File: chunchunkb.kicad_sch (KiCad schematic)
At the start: 116 parts, among them J1 Conn_01x02, SW1 SW_Push, SW10 SW_Push, SW11 SW_Push, SW12 SW_Push, SW13 SW_Push, SW14 SW_Push, SW15 SW_Push, SW16 SW_Push, SW17 SW_Push, SW18 SW_Push, SW19 SW_Push, SW2 SW_Push, SW20 SW_Push, SW21 SW_Push, SW22 SW_Push, SW23 SW_Push, SW24 SW_Push, SW25 SW_Push, SW26 SW_Push, SW27 SW_Push, SW28 SW_Push, SW29 SW_Push, SW3 SW_Push, SW30 SW_Push, SW31 EC11, SW32 SW_Push, SW33 SW_Push, SW34 SW_Push, SW35 SW_Push, SW36 SW_Push, SW4 SW_Push, SW5 SW_Push, SW6 SW_Push, SW7 SW_Push, SW8 SW_Push, SW9 SW_Push

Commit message: chore: reroute
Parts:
- LED1, LED10, LED11, LED12, LED13, LED14, LED15, LED16, LED17, LED18, LED19, LED2, LED20, LED21, LED22, LED23, LED24, LED25, LED26, LED27, LED28, LED29, LED3, LED30, LED31, LED32, LED33, LED34, LED35, LED4, LED5, LED6, LED7, LED8, LED9: value SK6812MINI-E -> YS-SK6812MINI-E
- SW31: footprint Rotary_Encoder:RotaryEncoder_Alps_EC11E-Switch_Vertical_H20mm -> kbd:keyswitch_cherrymx_hotswap_1u_rotary_encoder_ec12
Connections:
- net at LED13.2 (DOUT): now also LED14.4 (DIN); no longer LED12.2 (DOUT)
- net at LED31.4 (DIN): now also LED30.2 (DOUT); no longer LED30.4 (DIN)
- net at LED26.2 (DOUT): now also LED27.4 (DIN); no longer LED25.4 (DIN)
- net at LED27.2 (DOUT): now also LED28.4 (DIN); no longer LED26.4 (DIN)
- net at LED19.4 (DIN): now also LED18.2 (DOUT); no longer LED18.4 (DIN)
- net at LED25.2 (DOUT): now also LED26.4 (DIN); no longer LED24.2 (DOUT)
- net at LED15.2 (DOUT): now also LED16.4 (DIN); no longer LED14.4 (DIN)
- net at LED15.4 (DIN): now also LED14.2 (DOUT); no longer LED16.2 (DOUT)
- net at LED29.4 (DIN): now also LED28.2 (DOUT); no longer LED30.2 (DOUT)
- net at LED29.2 (DOUT): now also LED30.4 (DIN); no longer LED28.4 (DIN)
- net at LED13.4 (DIN): now also LED12.2 (DOUT); no longer LED14.2 (DOUT)
- net at LED17.4 (DIN): now also LED16.2 (DOUT); no longer LED18.2 (DOUT)
- net at LED17.2 (DOUT): now also LED18.4 (DIN); no longer LED16.4 (DIN)
- new net: LED24.2 (DOUT), LED25.4 (DIN)

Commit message: dual pcb
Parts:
- added D37, D38, D39, D40, D41, D42, D43, D44, D45, D46, D47, D48, D49, D50, D51, D52, D53, D54, D55, D56, D57, D58, D59, D60, D61, D62, D63, D64, D65, D66, D67, D68, D69, D70, D71, D72: 1N4148W, Diode_SMD:D_SOD-123, symbol Diode:1N4148W
- added Display2: nice!view, chunchunkb:nice_view, symbol nice_view:nice!view
- added H5, H6, H7, H8: MountingHole, MountingHole:MountingHole_2.2mm_M2_Pad, symbol Mechanical:MountingHole
- added J2: Conn_01x02, Connector_Molex:Molex_CLIK-Mate_502382-0270_1x02-1MP_P1.25mm_Vertical, symbol Connector_Generic:Conn_01x02
- added LED36, LED37, LED38, LED39, LED40, LED41, LED42, LED43, LED44, LED45, LED46, LED47, LED48, LED49, LED50, LED51, LED52, LED53, LED54, LED55, LED56, LED57, LED58, LED59, LED60, LED61, LED62, LED63, LED64, LED65, LED66, LED67, LED68, LED69, LED70: YS-SK6812MINI-E, chunchunkb:kbd.YS-SK6812MINI-E, symbol kbd:YS-SK6812MINI-E
- added MCU2: nice_nano, chunchunkb:kbd.ProMicro, symbol nice_nano:nice_nano
- added SW37, SW38, SW39, SW40, SW41, SW42, SW43, SW44, SW45, SW46, SW47, SW48, SW49, SW50, SW51, SW52, SW53, SW54, SW55, SW56, SW57, SW58, SW59, SW60, SW61, SW62, SW63, SW64, SW65, SW66, SW68, SW69, SW70, SW71, SW72: SW_Push, chunchunkb:kbd.keyswitch_cherrymx_hotswap_1u, symbol Switch:SW_Push
- added SW67: EC11, chunchunkb:RotaryEncoder_Alps_EC11E-Switch_Vertical_H20mm, symbol Device:RotaryEncoder_Switch
- added SW_POWER2: SW_SPDT, Button_Switch_SMD:SW_SPDT_PCM12, symbol Switch:SW_SPDT
- added SW_RST2: SW_Push, Button_Switch_SMD:SW_Tactile_SPST_NO_Straight_CK_PTS636Sx25SMTRLFS, symbol Switch:SW_Push
- Display1: footprint nice_view:nice_view -> chunchunkb:nice_view
- LED1, LED10, LED11, LED12, LED13, LED14, LED15, LED16, LED17, LED18, LED19, LED2, LED20, LED21, LED22, LED23, LED24, LED25, LED26, LED27, LED28, LED29, LED3, LED30, LED31, LED32, LED33, LED34, LED35, LED4, LED5, LED6, LED7, LED8, LED9: footprint kbd:YS-SK6812MINI-E -> chunchunkb:kbd.YS-SK6812MINI-E
- MCU1: footprint kbd:ProMicro -> chunchunkb:kbd.ProMicro
- SW1, SW10, SW11, SW12, SW13, SW14, SW15, SW16, SW17, SW18, SW19, SW2, SW20, SW21, SW22, SW23, SW24, SW25, SW26, SW27, SW28, SW29, SW3, SW30, SW32, SW33, SW34, SW35, SW36, SW4, SW5, SW6, SW7, SW8, SW9: footprint kbd:keyswitch_cherrymx_hotswap_1u -> chunchunkb:kbd.keyswitch_cherrymx_hotswap_1u
- SW31: footprint kbd:keyswitch_cherrymx_hotswap_1u_rotary_encoder_ec12 -> chunchunkb:RotaryEncoder_Alps_EC11E-Switch_Vertical_H20mm
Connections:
- net +BATT renamed +BATT L
- net COL 0 renamed COL 0 L
- net COL 1 renamed COL 1 L
- net COL 2 renamed COL 2 L
- net COL 3 renamed COL 3 L
- net COL 4 renamed COL 4 L
- net COL 5 renamed COL 5 L
- net CS renamed CS L
- net ENC A renamed ENC A L
- net ENC B renamed ENC B L
- net LED renamed LED L
- net MOSI renamed MOSI L
- net ROW 0 renamed ROW 0 L
- net ROW 1 renamed ROW 1 L
- net ROW 2 renamed ROW 2 L
- net ROW 3 renamed ROW 3 L
- net ROW 4 renamed ROW 4 L
- net ROW 5 renamed ROW 5 L
- net SCK renamed SCK L
- net VCC renamed VCC L
- new net: D58.2 (A), SW58.2
- new net: LED68.2 (DOUT), LED69.4 (DIN)
- new net: LED67.2 (DOUT), LED68.4 (DIN)
- new net: LED51.2 (DOUT), LED52.4 (DIN)
- new net: LED50.2 (DOUT), LED51.4 (DIN)
- new net: D70.2 (A), SW70.2
- new net: D38.2 (A), SW38.2
- new net: D55.2 (A), SW55.2
- new net: D59.2 (A), SW59.2
- new net: D62.2 (A), SW62.2
- new net: LED36.2 (DOUT), LED37.4 (DIN)
- new net: D37.2 (A), SW37.2
- new net: D42.2 (A), SW42.2
- new net: LED54.2 (DOUT), LED55.4 (DIN)
- new net: LED53.2 (DOUT), LED54.4 (DIN)
- new net: LED55.2 (DOUT), LED56.4 (DIN)
- new net: LED45.2 (DOUT), LED46.4 (DIN)
- new net: LED44.2 (DOUT), LED45.4 (DIN)
- new net: MCU2.22 (RST), SW_RST2.1
- new net: D60.2 (A), SW60.2
- new net: LED59.2 (DOUT), LED60.4 (DIN)
- new net: LED58.2 (DOUT), LED59.4 (DIN)
- new net: D44.2 (A), SW44.2
- new net: D46.2 (A), SW46.2
- new net: D72.2 (A), SW72.2
- new net: LED49.2 (DOUT), LED50.4 (DIN)
- new net: LED48.2 (DOUT), LED49.4 (DIN)
- new net: LED69.2 (DOUT), LED70.4 (DIN)
- new net: LED63.2 (DOUT), LED64.4 (DIN)
- new net: LED62.2 (DOUT), LED63.4 (DIN)
- new net: D43.2 (A), SW43.2
- new net: D56.2 (A), SW56.2
- new net: D52.2 (A), SW52.2
- new net: LED47.2 (DOUT), LED48.4 (DIN)
- new net: LED46.2 (DOUT), LED47.4 (DIN)
- new net: LED65.2 (DOUT), LED66.4 (DIN)
- new net: LED64.2 (DOUT), LED65.4 (DIN)
- new net: LED39.2 (DOUT), LED40.4 (DIN)
- new net: LED38.2 (DOUT), LED39.4 (DIN)
- new net: LED37.2 (DOUT), LED38.4 (DIN)
- new net: LED57.2 (DOUT), LED58.4 (DIN)
- new net: LED56.2 (DOUT), LED57.4 (DIN)
- new net: LED41.2 (DOUT), LED42.4 (DIN)
- new net: LED40.2 (DOUT), LED41.4 (DIN)
- new net: D68.2 (A), SW68.2
- new net: D48.2 (A), SW48.2
- new net: D63.2 (A), SW63.2
- new net: LED66.2 (DOUT), LED67.4 (DIN)
- new net: MCU2.24 (BATIN/P0.04), SW_POWER2.2 (B)
- new net: D66.2 (A), SW66.2
- new net: D69.2 (A), SW69.2
- new net: D54.2 (A), SW54.2
- new net: D40.2 (A), SW40.2
- new net: LED43.2 (DOUT), LED44.4 (DIN)
- new net: D39.2 (A), SW39.2
- new net: LED52.2 (DOUT), LED53.4 (DIN)
- new net: D50.2 (A), SW50.2
- new net: D49.2 (A), SW49.2
- new net: D61.2 (A), SW61.2
- new net: D41.2 (A), SW41.2
- new net: D65.2 (A), SW65.2
- new net: LED42.2 (DOUT), LED43.4 (DIN)
- new net: D53.2 (A), SW53.2
- new net: D71.2 (A), SW71.2
- new net: D64.2 (A), SW64.2
- new net: D47.2 (A), SW47.2
- new net: LED61.2 (DOUT), LED62.4 (DIN)
- new net: LED60.2 (DOUT), LED61.4 (DIN)
- new net: D45.2 (A), SW45.2
- new net: D51.2 (A), SW51.2
- new net: D57.2 (A), SW57.2
- new net +BATT R: J2.1 (Pin_1), SW_POWER2.1 (A)
- new net COL 0 R: MCU2.18 (AIN0/P0.02), SW37.1, SW43.1, SW49.1, SW55.1, SW61.1, SW67.S1
- new net COL 1 R: MCU2.17 (P1.15), SW38.1, SW44.1, SW50.1, SW56.1, SW62.1, SW68.1
- new net COL 2 R: MCU2.16 (P1.13), SW39.1, SW45.1, SW51.1, SW57.1, SW63.1, SW69.1
- new net COL 3 R: MCU2.15 (P1.11), SW40.1, SW46.1, SW52.1, SW58.1, SW64.1, SW70.1
- new net COL 4 R: MCU2.14 (NFC2/P0.10), SW41.1, SW47.1, SW53.1, SW59.1, SW65.1, SW71.1
- new net COL 5 R: MCU2.13 (NFC1/P0.09), SW42.1, SW48.1, SW54.1, SW60.1, SW66.1, SW72.1
- new net CS R: Display2.5 (CS), MCU2.5 (P0.17)
- new net ENC A R: MCU2.20 (AIN7/P0.31), SW67.A
- new net ENC B R: MCU2.19 (AIN5/P0.29), SW67.B
- new net GND R: Display2.4 (GND), J2.2 (Pin_2), LED36.3 (GND_R), LED37.3 (GND_R), LED38.3 (GND_R), LED39.3 (GND_R), LED40.3 (GND_R), LED41.3 (GND_R), LED42.3 (GND_R), LED43.3 (GND_R), LED44.3 (GND_R), LED45.3 (GND_R), LED46.3 (GND_R), LED47.3 (GND_R), LED48.3 (GND_R), LED49.3 (GND_R), LED50.3 (GND_R), LED51.3 (GND_R), LED52.3 (GND_R), LED53.3 (GND_R), LED54.3 (GND_R), LED55.3 (GND_R), LED56.3 (GND_R), LED57.3 (GND_R), LED58.3 (GND_R), LED59.3 (GND_R), LED60.3 (GND_R), LED61.3 (GND_R), LED62.3 (GND_R), LED63.3 (GND_R), LED64.3 (GND_R), LED65.3 (GND_R), LED66.3 (GND_R), LED67.3 (GND_R), LED68.3 (GND_R), LED69.3 (GND_R), LED70.3 (GND_R), MCU2.23 (GND), MCU2.3 (GND), MCU2.4 (GND), SW67.C, SW_RST2.2
- new net LED R: LED36.4 (DIN), MCU2.2 (RX1/P0.08)
- new net MOSI R: Display2.1 (MOSI), MCU2.1 (TX0/P0.06)
- new net ROW 0 R: D37.1 (K), D38.1 (K), D39.1 (K), D40.1 (K), D41.1 (K), D42.1 (K), MCU2.7 (P0.22)
- new net ROW 1 R: D43.1 (K), D44.1 (K), D45.1 (K), D46.1 (K), D47.1 (K), D48.1 (K), MCU2.8 (P0.24)
- new net ROW 2 R: D49.1 (K), D50.1 (K), D51.1 (K), D52.1 (K), D53.1 (K), D54.1 (K), MCU2.9 (P1.00)
- new net ROW 3 R: D55.1 (K), D56.1 (K), D57.1 (K), D58.1 (K), D59.1 (K), D60.1 (K), MCU2.10 (P0.11)
- new net ROW 4 R: D61.1 (K), D62.1 (K), D63.1 (K), D64.1 (K), D65.1 (K), D66.1 (K), MCU2.11 (P1.04)
- new net ROW 5 R: D67.1 (K), D68.1 (K), D69.1 (K), D70.1 (K), D71.1 (K), D72.1 (K), MCU2.12 (P1.06)
- new net SCK R: Display2.2 (SCK), MCU2.6 (P0.20)
- new net SW67B: D67.2 (A), SW67.S2
- new net VCC R: Display2.3 (VCC), LED36.1 (VDD_R), LED37.1 (VDD_R), LED38.1 (VDD_R), LED39.1 (VDD_R), LED40.1 (VDD_R), LED41.1 (VDD_R), LED42.1 (VDD_R), LED43.1 (VDD_R), LED44.1 (VDD_R), LED45.1 (VDD_R), LED46.1 (VDD_R), LED47.1 (VDD_R), LED48.1 (VDD_R), LED49.1 (VDD_R), LED50.1 (VDD_R), LED51.1 (VDD_R), LED52.1 (VDD_R), LED53.1 (VDD_R), LED54.1 (VDD_R), LED55.1 (VDD_R), LED56.1 (VDD_R), LED57.1 (VDD_R), LED58.1 (VDD_R), LED59.1 (VDD_R), LED60.1 (VDD_R), LED61.1 (VDD_R), LED62.1 (VDD_R), LED63.1 (VDD_R), LED64.1 (VDD_R), LED65.1 (VDD_R), LED66.1 (VDD_R), LED67.1 (VDD_R), LED68.1 (VDD_R), LED69.1 (VDD_R), LED70.1 (VDD_R), MCU2.21 (VCC)
- no-connect marks 0 -> 10
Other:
- moved on the sheet: D1, D10, D11, D12, D13, D14, D15, D16, D17, D18, D19, D2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

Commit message: reversible
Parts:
- removed D37, D38, D39, D40, D41, D42, D43, D44, D45, D46, D47, D48, D49, D50, D51, D52, D53, D54, D55, D56, D57, D58, D59, D60, D61, D62, D63, D64, D65, D66, D67, D68, D69, D70, D71, D72: 1N4148W, Diode_SMD:D_SOD-123, symbol Diode:1N4148W
- removed Display1, Display2: nice!view, chunchunkb:nice_view, symbol nice_view:nice!view
- removed H5, H6, H7, H8: MountingHole, MountingHole:MountingHole_2.2mm_M2_Pad, symbol Mechanical:MountingHole
- removed J2: Conn_01x02, Connector_Molex:Molex_CLIK-Mate_502382-0270_1x02-1MP_P1.25mm_Vertical, symbol Connector_Generic:Conn_01x02
- removed LED36, LED37, LED38, LED39, LED40, LED41, LED42, LED43, LED44, LED45, LED46, LED47, LED48, LED49, LED50, LED51, LED52, LED53, LED54, LED55, LED56, LED57, LED58, LED59, LED60, LED61, LED62, LED63, LED64, LED65, LED66, LED67, LED68, LED69, LED70: YS-SK6812MINI-E, chunchunkb:kbd.YS-SK6812MINI-E, symbol kbd:YS-SK6812MINI-E
- removed MCU1, MCU2: nice_nano, chunchunkb:kbd.ProMicro, symbol nice_nano:nice_nano
- removed SW37, SW38, SW39, SW40, SW41, SW42, SW43, SW44, SW45, SW46, SW47, SW48, SW49, SW50, SW51, SW52, SW53, SW54, SW55, SW56, SW57, SW58, SW59, SW60, SW61, SW62, SW63, SW64, SW65, SW66, SW68, SW69, SW70, SW71, SW72: SW_Push, chunchunkb:kbd.keyswitch_cherrymx_hotswap_1u, symbol Switch:SW_Push
- removed SW67: EC11, chunchunkb:RotaryEncoder_Alps_EC11E-Switch_Vertical_H20mm, symbol Device:RotaryEncoder_Switch
- removed SW_POWER2: SW_SPDT, Button_Switch_SMD:SW_SPDT_PCM12, symbol Switch:SW_SPDT
- removed SW_RST2: SW_Push, Button_Switch_SMD:SW_Tactile_SPST_NO_Straight_CK_PTS636Sx25SMTRLFS, symbol Switch:SW_Push
- added J2: OLED, chunchunkb:nice_view, symbol Connector_Generic:Conn_01x05
- added JP1, JP2, JP3, JP4, JP5, JP6, JP7, JP8: jumper, chunchunkb:Jumper, symbol chunchunkb:jumper
- added U1: (no value), chunchunkb:ProMicro_DUAL, symbol Keyboard_CS:NRF_micro_jumper
- D1, D10, D11, D12, D13, D14, D15, D16, D17, D18, D19, D2, D20, D21, D22, D23, D24, D25, D26, D27, D28, D29, D3, D30, D31, D32, D33, D34, D35, D36, D4, D5, D6, D7, D8, D9: footprint Diode_SMD:D_SOD-123 -> chunchunkb:D_SOD-123
- J1: value Conn_01x02 -> BATT; footprint Connector_Molex:Molex_CLIK-Mate_502382-0270_1x02-1MP_P1.25mm_Vertical -> chunchunkb:MX1.25mm
- LED1, LED10, LED11, LED12, LED13, LED14, LED15, LED16, LED17, LED18, LED19, LED2, LED20, LED21, LED22, LED23, LED24, LED25, LED26, LED27, LED28, LED29, LED3, LED30, LED31, LED32, LED33, LED34, LED35, LED4, LED5, LED6, LED7, LED8, LED9: footprint chunchunkb:kbd.YS-SK6812MINI-E -> chunchunkb:YS-SK6812MINI-E
- SW1, SW10, SW11, SW12, SW13, SW14, SW15, SW16, SW17, SW18, SW19, SW2, SW20, SW21, SW22, SW23, SW24, SW25, SW26, SW27, SW28, SW29, SW3, SW30, SW32, SW33, SW34, SW35, SW36, SW4, SW5, SW6, SW7, SW8, SW9: footprint chunchunkb:kbd.keyswitch_cherrymx_hotswap_1u -> chunchunkb:MX-1U-Hotswap
- SW31: footprint chunchunkb:RotaryEncoder_Alps_EC11E-Switch_Vertical_H20mm -> chunchunkb:EC11_Switch
- SW_POWER1: value SW_SPDT -> SW_POWER; footprint Button_Switch_SMD:SW_SPDT_PCM12 -> chunchunkb:SW_SPDT_PCM12
- SW_RST1: value SW_PUSH -> SW_RST; footprint Button_Switch_SMD:SW_Tactile_SPST_NO_Straight_CK_PTS636Sx25SMTRLFS -> Button_Switch_THT:SW_PUSH_1P1T_6x3.5mm_H4.3_APEM_MJTP1243
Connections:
- net GND: now also JP2.2 (B), JP6.2 (B), U1.23 (GND), U1.3 (GND), U1.4 (GND)
- net COL 5: now reaches SW36.2
- net COL 5: now also SW12.2, SW18.2, SW24.2, SW30.2, SW6.2, U1.13 (B6/10); no longer D36.2 (A)
- net ROW 4: now reaches D30.2 (A)
- net ROW 4: now also D25.2 (A), D26.2 (A), D27.2 (A), D28.2 (A), D29.2 (A), U1.11 (8/B4); no longer SW30.2
- net ROW 1: now reaches D12.2 (A)
- net ROW 1: now also D10.2 (A), D11.2 (A), D7.2 (A), D8.2 (A), D9.2 (A), U1.8 (5/C6); no longer SW12.2
- net COL 3: now reaches SW28.2
- net COL 3: now also SW10.2, SW16.2, SW22.2, SW34.2, SW4.2, U1.15 (B3/14); no longer D28.2 (A)
- net COL 4: now reaches SW17.2
- net COL 4: now also SW11.2, SW23.2, SW29.2, SW35.2, SW5.2, U1.14 (B2/16); no longer D17.2 (A)
- net ROW 3: now reaches D23.2 (A)
- net ROW 3: now also D19.2 (A), D20.2 (A), D21.2 (A), D22.2 (A), D24.2 (A), U1.10 (7/E6); no longer SW23.2
- net COL 1: now reaches SW8.2
- net COL 1: now also SW14.2, SW2.2, SW20.2, SW26.2, SW32.2, U1.17 (F7/A0); no longer D8.2 (A)
- net ROW 0: now reaches D6.2 (A)
- net ROW 0: now also D1.2 (A), D2.2 (A), D3.2 (A), D4.2 (A), D5.2 (A), U1.7 (4/D4); no longer SW6.2
- net ROW 5: now reaches D32.2 (A)
- net ROW 5: now also D31.2 (A), D33.2 (A), D34.2 (A), D35.2 (A), D36.2 (A), U1.12 (9/B5); no longer SW32.2
- net ROW 2: now reaches D16.2 (A)
- net ROW 2: now also D13.2 (A), D14.2 (A), D15.2 (A), D17.2 (A), D18.2 (A), U1.9 (6/D7); no longer SW16.2
- net COL 2: now reaches SW33.2
- net COL 2: now also SW15.2, SW21.2, SW27.2, SW3.2, SW9.2, U1.16 (B1/15); no longer D33.2 (A)
- net at SW_POWER1.2 (B): now also U1.24 (RAW)
- net COL 0: now reaches SW13.2
- net COL 0: now also SW1.2, SW19.2, SW25.2, SW31.S2, SW7.2, U1.18 (F6/A1); no longer D13.2 (A)
- net RESET: now reaches SW_RST1.1
- net RESET: now also U1.22 (RST)
- net +BATT L: no longer names the net of J1.1 (Pin_1), SW_POWER1.1 (A)
- removed net COL 0 L: SW1.1, SW13.1, SW19.1, SW25.1, SW31.S1, SW7.1
- removed net COL 1 L: SW14.1, SW2.1, SW20.1, SW26.1, SW32.1, SW8.1
- removed net COL 2 L: SW15.1, SW21.1, SW27.1, SW3.1, SW33.1, SW9.1
- removed net COL 3 L: SW10.1, SW16.1, SW22.1, SW28.1, SW34.1, SW4.1
- removed net COL 4 L: SW11.1, SW17.1, SW23.1, SW29.1, SW35.1, SW5.1
- removed net COL 5 L: SW12.1, SW18.1, SW24.1, SW30.1, SW36.1, SW6.1
- net ENC A L renamed ENC A
- net ENC A: now also U1.20 (F4/A3)
- net ENC B L renamed ENC B
- net ENC B: now also U1.19 (F5/A2)
- net LED L renamed LED
- net LED: now also U1.2 (RX1/D2)
- removed net ROW 0 L: D1.1 (K), D2.1 (K), D3.1 (K), D4.1 (K), D5.1 (K), D6.1 (K)
- removed net ROW 1 L: D10.1 (K), D11.1 (K), D12.1 (K), D7.1 (K), D8.1 (K), D9.1 (K)
- removed net ROW 2 L: D13.1 (K), D14.1 (K), D15.1 (K), D16.1 (K), D17.1 (K), D18.1 (K)
- removed net ROW 3 L: D19.1 (K), D20.1 (K), D21.1 (K), D22.1 (K), D23.1 (K), D24.1 (K)
- removed net ROW 4 L: D25.1 (K), D26.1 (K), D27.1 (K), D28.1 (K), D29.1 (K), D30.1 (K)
- removed net ROW 5 L: D31.1 (K), D32.1 (K), D33.1 (K), D34.1 (K), D35.1 (K), D36.1 (K)
- removed net SW31B: D31.2 (A), SW31.S2
- net VCC L renamed VCC
- net VCC: now also J2.3 (Pin_3), U1.21 (VCC)
- new net: D14.1 (K), SW14.1
- new net: D25.1 (K), SW25.1
- new net: D23.1 (K), SW23.1
- new net: D30.1 (K), SW30.1
- new net: D4.1 (K), SW4.1
- new net: D10.1 (K), SW10.1
- new net: D27.1 (K), SW27.1
- new net: D8.1 (K), SW8.1
- new net: J2.5 (Pin_5), JP1.1 (A), JP8.1 (A)
- new net: D17.1 (K), SW17.1
- new net: D16.1 (K), SW16.1
- new net: D6.1 (K), SW6.1
- new net: D13.1 (K), SW13.1
- new net: D26.1 (K), SW26.1
- new net: D5.1 (K), SW5.1
- new net: D24.1 (K), SW24.1
- new net: D35.1 (K), SW35.1
- new net: D36.1 (K), SW36.1
- new net: J2.2 (Pin_2), JP3.1 (A), JP6.1 (A)
- new net: D32.1 (K), SW32.1
- new net: D3.1 (K), SW3.1
- new net: D12.1 (K), SW12.1
- new net: D19.1 (K), SW19.1
- new net: D21.1 (K), SW21.1
- new net: D7.1 (K), SW7.1
- new net: D28.1 (K), SW28.1
- new net: D33.1 (K), SW33.1
- new net: D20.1 (K), SW20.1
- new net: D2.1 (K), SW2.1
- new net: D11.1 (K), SW11.1
- new net: D29.1 (K), SW29.1
- new net: D15.1 (K), SW15.1
- new net: J2.4 (Pin_4), JP2.1 (A), JP7.1 (A)
- new net: D9.1 (K), SW9.1
- new net: J2.1 (Pin_1), JP4.1 (A), JP5.1 (A)
- new net: D18.1 (K), SW18.1
- new net: D22.1 (K), SW22.1
- new net: D1.1 (K), SW1.1
- new net: D34.1 (K), SW34.1
- new net CS: JP1.2 (B), JP5.2 (B), U1.1 (TX0/D3)
- new net MOSI/SDA: JP3.2 (B), JP7.2 (B), U1.5 (2/D1/SDA)
- new net SCK/SCL: JP4.2 (B), JP8.2 (B), U1.6 (3/D0/SCL)
- new net SW31A: D31.1 (K), SW31.S1
- no-connect marks 10 -> 3
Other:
- moved on the sheet: D1, H1, H2, H3, H4, J1, LED1, LED10, LED11, LED12, LED13, LED14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

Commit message: reroute
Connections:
- net GND: now also U1.26 (GND)
- net at SW_POWER1.2 (B), U1.24 (RAW): now also U1.25 (BAT+)
- no-connect marks 3 -> 2
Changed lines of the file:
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@@
 	)
 	(junction
-		(at 30.48 48.26)
-		(diameter 0)
-		(color 0 0 0 0)
-	)
-	(junction
 		(at 295.91 114.3)
 		(diameter 0)
@@
 	)
 	(junction
+		(at 30.48 48.26)
+		(diameter 0)
+		(color 0 0 0 0)
+	)
+	(junction
 		(at 337.82 43.18)
 		(diameter 0)
@@
 	)
 	(junction
+		(at 25.4 48.26)
+		(diameter 0)
+		(color 0 0 0 0)
+	)
+	(junction
 		(at 323.85 43.18)
 		(diameter 0)
@@
 	)
 	(junction
+		(at 73.66 43.18)
+		(diameter 0)
+		(color 0 0 0 0)
+	)
+	(junction
 		(at 347.98 88.9)
 		(diameter 0)
@@
 	)
 	(no_connect
-		(at 71.12 40.64)
-	)
-	(no_connect
 		(at 101.6 45.72)
 	)
@@
 	(wire
 		(pts
+			(xy 25.4 48.26) (xy 30.48 48.26)
+		)
+		(stroke
+			(width 0)
+			(type default)
+		)
+	)
+	(wire
+		(pts
 			(xy 337.82 60.96) (xy 351.79 60.96)
 		)
@@
 	(wire
 		(pts
+			(xy 71.12 40.64) (xy 73.66 40.64)
+		)
+		(stroke
+			(width 0)
+			(type default)
+		)
+	)
+	(wire
+		(pts
 			(xy 306.07 35.56) (xy 306.07 53.34)
 		)
@@
 	(wire
 		(pts
+			(xy 25.4 40.64) (xy 25.4 48.26)
+		)
+		(stroke
+			(width 0)
+			(type default)
+		)
+	)
+	(wire
+		(pts
 			(xy 347.98 35.56) (xy 347.98 53.34)
 		)
@@
 	(wire
 		(pts
-			(xy 27.94 48.26) (xy 30.48 48.26)
+			(xy 19.05 48.26) (xy 25.4 48.26)
 		)
 		(stroke
@@
 	(wire
 		(pts
+			(xy 73.66 43.18) (xy 71.12 43.18)
+		)
+		(stroke
+			(width 0)
+			(type default)
+		)
+	)
+	(wire
+		(pts
 			(xy 361.95 124.46) (xy 361.95 133.35)
 		)
@@
 	(wire
 		(pts
-			(xy 91.44 43.18) (xy 71.12 43.18)
+			(xy 73.66 40.64) (xy 73.66 43.18)
+		)
+		(stroke
+			(width 0)
+			(type default)
+		)
+	)
+	(wire
+		(pts
+			(xy 91.44 43.18) (xy 73.66 43.18)
 		)
 		(stroke
@@
 	(wire
 		(pts
+			(xy 35.56 40.64) (xy 25.4 40.64)
+		)
+		(stroke
+			(width 0)
+			(type default)
+		)
+	)
+	(wire
+		(pts
 			(xy 54.61 187.96) (xy 58.42 187.96)
 		)
@@
 	(symbol
 		(lib_id "power:GND")
-		(at 27.94 48.26 270)
+		(at 19.05 48.26 270)
 		(unit 1)
 		(body_style 1)
@@
 		(dnp no)
 		(property "Reference" "#PWR06"
-			(at 21.59 48.26 0)
+			(at 12.7 48.26 0)
 			(hide yes)
 			(show_name no)
@@
 		)
 		(property "Value" "GND"
-			(at 22.86 51.054 90)
+			(at 13.97 51.054 90)
 			(show_name no)
 			(do_not_autoplace no)
@@
 		)
 		(property "Footprint" ""
-			(at 27.94 48.26 0)
+			(at 19.05 48.26 0)
 			(hide yes)
 			(show_name no)
@@
 		)
 		(property "Datasheet" ""
-			(at 27.94 48.26 0)
+			(at 19.05 48.26 0)
 			(hide yes)
 			(show_name no)
@@
 		)
 		(property "Description" "Power symbol creates a global label with name \"GND\" , ground"
-			(at 27.94 48.26 0)
+			(at 19.05 48.26 0)
 			(hide yes)
 			(show_name no)

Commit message: feat: resize via, rerouting
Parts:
- SW_RST1: footprint Button_Switch_THT:SW_PUSH_1P1T_6x3.5mm_H4.3_APEM_MJTP1243 -> chunchunkb:SW_PUSH_1P1T_6x3.5mm_H4.3_APEM_MJTP1243
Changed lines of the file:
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@@
 			)
 		)
-		(property "Footprint" "Button_Switch_THT:SW_PUSH_1P1T_6x3.5mm_H4.3_APEM_MJTP1243"
+		(property "Footprint" "chunchunkb:SW_PUSH_1P1T_6x3.5mm_H4.3_APEM_MJTP1243"
 			(at 162.56 39.37 0)
 			(hide yes)

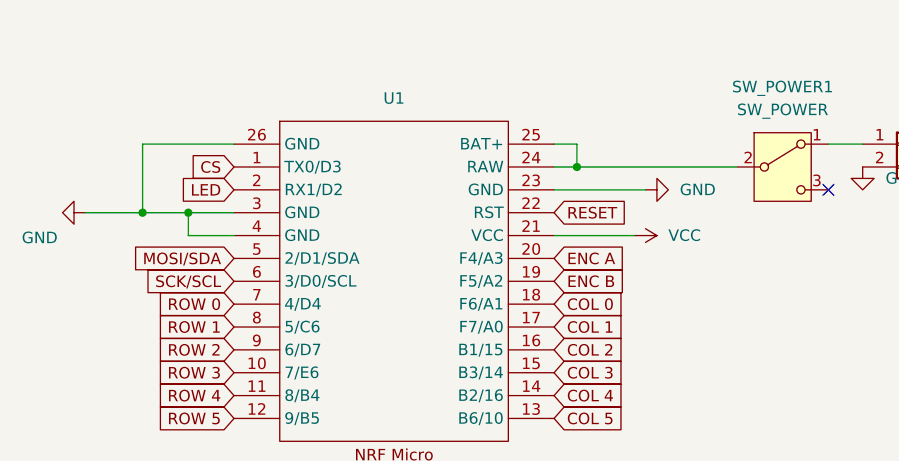
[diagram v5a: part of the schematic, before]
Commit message: fix switch footprint
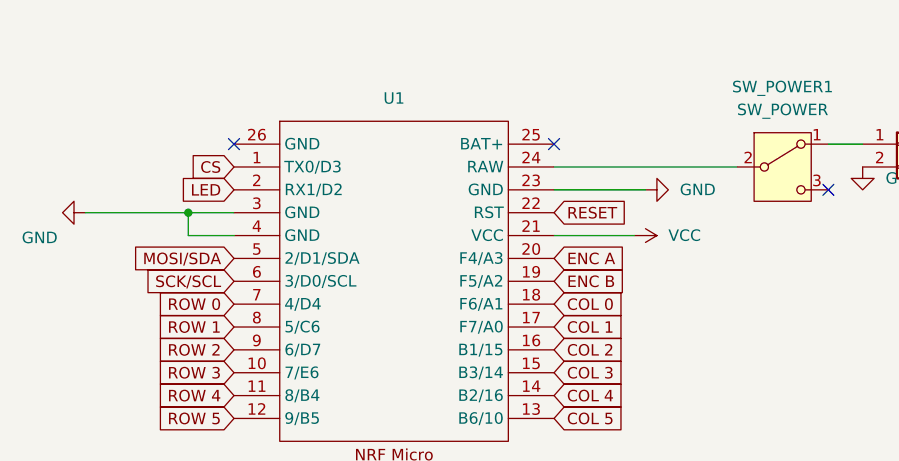
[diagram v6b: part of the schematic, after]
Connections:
- net GND: no longer U1.26 (GND)
- net at SW_POWER1.2 (B), U1.24 (RAW): no longer U1.25 (BAT+)
- no-connect marks 2 -> 4
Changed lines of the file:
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@@
-	)
-	(junction
-		(at 25.4 48.26)
-		(diameter 0)
-		(color 0 0 0 0)
 	)
 	(junction
@@
 	(junction
 		(at 361.95 106.68)
-		(diameter 0)
-		(color 0 0 0 0)
-	)
-	(junction
-		(at 73.66 43.18)
 		(diameter 0)
 		(color 0 0 0 0)
@@
 		(at 58.42 203.2)
 	)
+	(no_connect
+		(at 35.56 40.64)
+	)
+	(no_connect
+		(at 71.12 40.64)
+	)
 	(wire
 		(pts
@@
 	(wire
 		(pts
-			(xy 25.4 48.26) (xy 30.48 48.26)
+			(xy 19.05 48.26) (xy 30.48 48.26)
 		)
 		(stroke
@@
 	(wire
 		(pts
-			(xy 71.12 40.64) (xy 73.66 40.64)
-		)
-		(stroke
-			(width 0)
-			(type default)
-		)
-	)
-	(wire
-		(pts
 			(xy 306.07 35.56) (xy 306.07 53.34)
 		)
@@
 	(wire
 		(pts
-			(xy 25.4 40.64) (xy 25.4 48.26)
-		)
-		(stroke
-			(width 0)
-			(type default)
-		)
-	)
-	(wire
-		(pts
 			(xy 347.98 35.56) (xy 347.98 53.34)
 		)
@@
 	(wire
 		(pts
-			(xy 19.05 48.26) (xy 25.4 48.26)
-		)
-		(stroke
-			(width 0)
-			(type default)
-		)
-	)
-	(wire
-		(pts
 			(xy 309.88 96.52) (xy 323.85 96.52)
 		)
@@
 	(wire
 		(pts
-			(xy 73.66 43.18) (xy 71.12 43.18)
+			(xy 71.12 43.18) (xy 91.44 43.18)
 		)
 		(stroke
@@
 	(wire
 		(pts
-			(xy 73.66 40.64) (xy 73.66 43.18)
-		)
-		(stroke
-			(width 0)
-			(type default)
-		)
-	)
-	(wire
-		(pts
-			(xy 91.44 43.18) (xy 73.66 43.18)
-		)
-		(stroke
-			(width 0)
-			(type default)
-		)
-	)
-	(wire
-		(pts
 			(xy 279.4 78.74) (xy 281.94 78.74)
 		)
@@
 		)
 		(stroke
-			(width 0)
-			(type default)
-		)
-	)
-	(wire
-		(pts
-			(xy 35.56 40.64) (xy 25.4 40.64)
-		)
-		(stroke

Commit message: feat: add case
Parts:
- H1, H2, H3, H4: footprint MountingHole:MountingHole_2.2mm_M2_Pad -> chunchunkb:HOLE_M2_TH
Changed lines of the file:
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@@
 			)
 		)
-		(property "Footprint" "MountingHole:MountingHole_2.2mm_M2_Pad"
+		(property "Footprint" "chunchunkb:HOLE_M2_TH"
 			(at 17.78 271.78 0)
 			(hide yes)
@@
 			)
 		)
-		(property "Footprint" "MountingHole:MountingHole_2.2mm_M2_Pad"
+		(property "Footprint" "chunchunkb:HOLE_M2_TH"
 			(at 17.78 278.13 0)
 			(hide yes)
@@
 			)
 		)
-		(property "Footprint" "MountingHole:MountingHole_2.2mm_M2_Pad"
+		(property "Footprint" "chunchunkb:HOLE_M2_TH"
 			(at 17.78 257.81 0)
 			(hide yes)
@@
 			)
 		)
-		(property "Footprint" "MountingHole:MountingHole_2.2mm_M2_Pad"
+		(property "Footprint" "chunchunkb:HOLE_M2_TH"
 			(at 17.78 264.16 0)
 			(hide yes)
